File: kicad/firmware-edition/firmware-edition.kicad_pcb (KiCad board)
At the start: 2 copper layers, 70.4 x 63.5 mm, 102 parts, among them J1 Solar Panel, J10 GPIO, J11 I2C-3V3, J12 GPIO, J13 SPI, J14 I2C-5V, J15 SWD, J16 Conn_01x03, J17 Conn_01x01_Pin, J18 Conn_01x01_Pin, J19 Conn_01x01_Pin, J2 BATT, J20 Conn_01x01_Pin, J21 GPIO, J22 3V3, J3 3V3 Sensor Bus, J5 Conn_01x01_Pin, J6 Conn_01x01_Pin, J8 GPIO, J9 Conn_01x01_Pin, Q1 BSS84, Q2 BSS84, Q3 BSS84, SW1 BOOT_DFU, SW2 RST, U1 ADP5091, U2 TPS61023DRLR, U3 MAX-M10M-00B, U4 Si4463, U5 STM32U073KCU6, U6 TXS0102VDCTR, Y1 30MHz

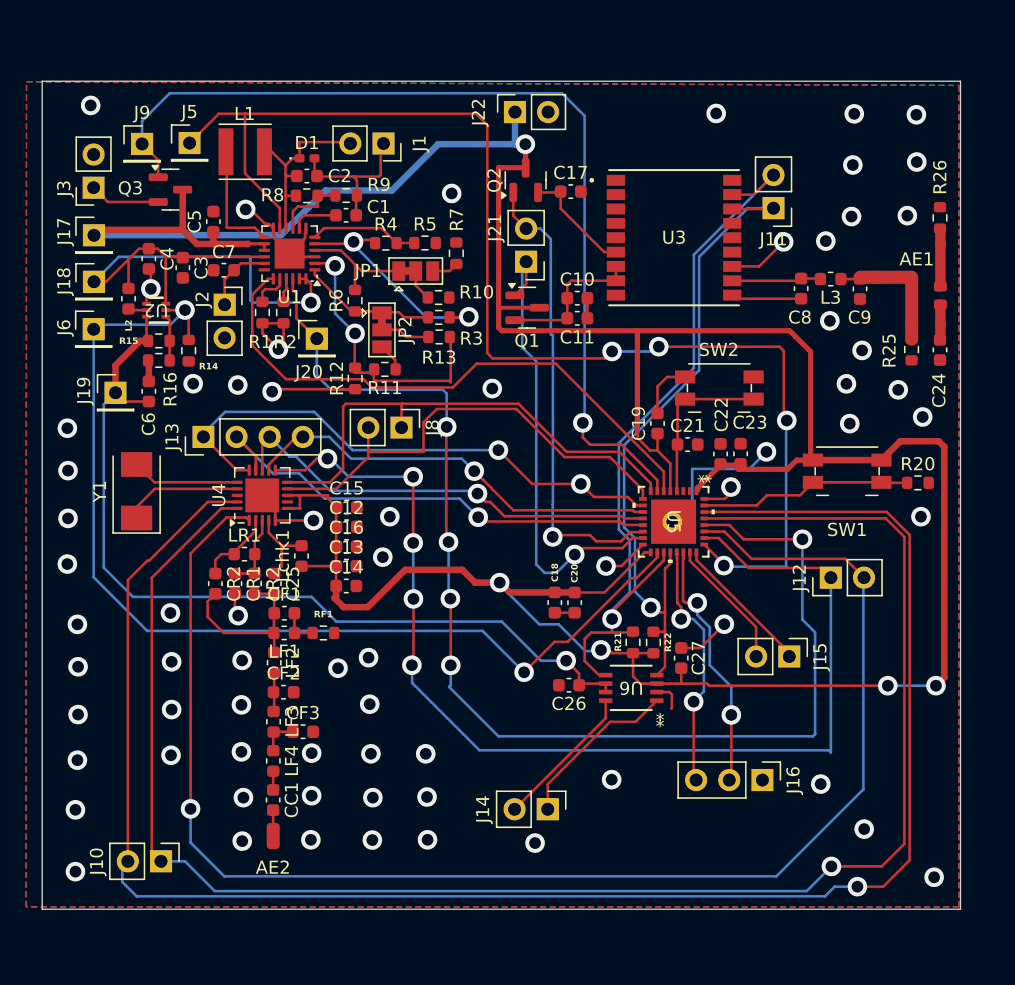
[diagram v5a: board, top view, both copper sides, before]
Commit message: main board updates, stm breakout
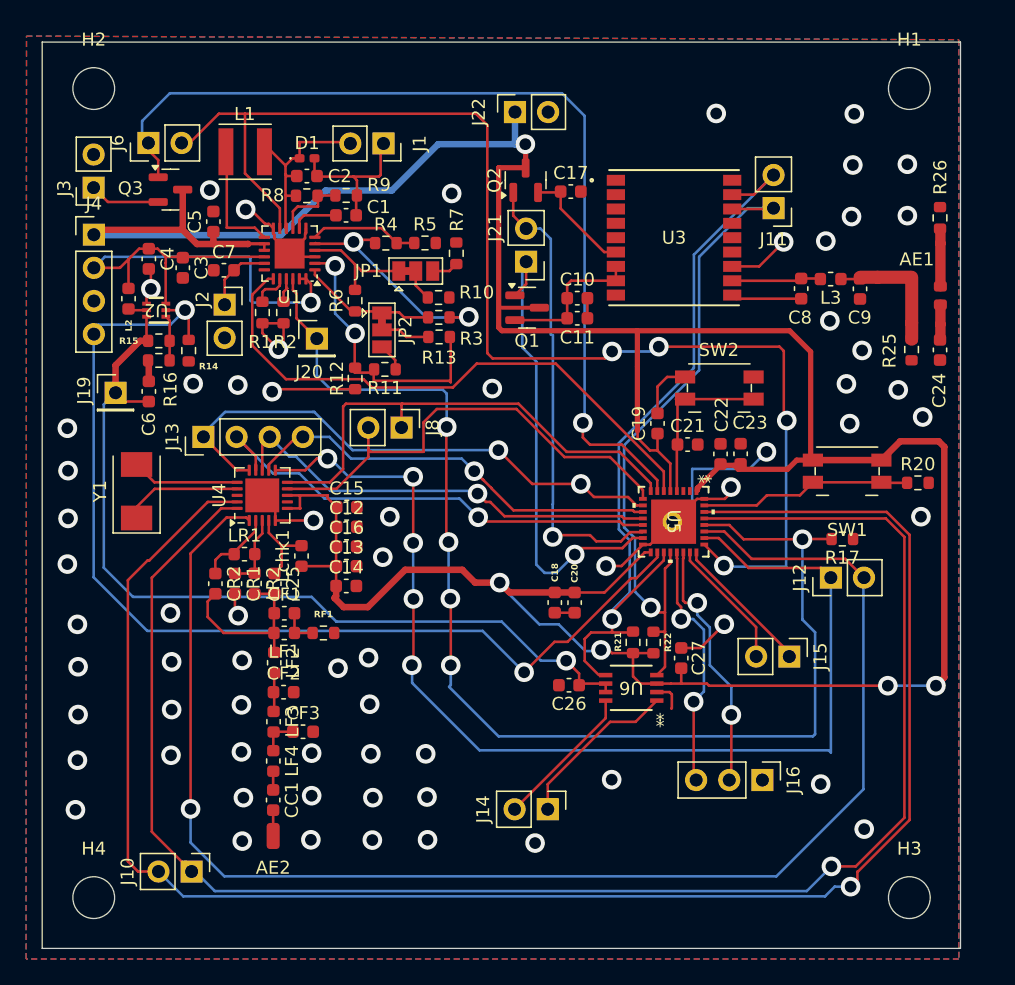
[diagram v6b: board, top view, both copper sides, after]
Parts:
- removed J17, J18, J5, J9: Conn_01x01_Pin, Connector_PinHeader_2.54mm:PinHeader_1x01_P2.54mm_Vertical
- added H1: MountingHole, MountingHole:MountingHole_3.2mm_M3_ISO14580, F.Cu at (175.0, 65.0)
- added H2: MountingHole, MountingHole:MountingHole_3.2mm_M3_ISO14580, F.Cu at (112.5, 65.0)
- added H3: MountingHole, MountingHole:MountingHole_3.2mm_M3_ISO14580, F.Cu at (175.0, 127.0)
- added H4: MountingHole, MountingHole:MountingHole_3.2mm_M3_ISO14580, F.Cu at (112.5, 127.0)
- added J4: Conn_01x04, Connector_PinHeader_2.54mm:PinHeader_1x04_P2.54mm_Vertical, F.Cu at (112.5, 76.2)
- added R17: 1M, Resistor_SMD:R_0603_1608Metric, F.Cu at (169.9, 99.5)
- J6: value Conn_01x01_Pin -> Conn_01x02; footprint Connector_PinHeader_2.54mm:PinHeader_1x01_P2.54mm_Vertical -> Connector_PinHeader_2.54mm:PinHeader_1x02_P2.54mm_Vertical
- moved J6 14.9 mm to (116.7, 69.2), turned to 90 degrees
- moved J10 2.47 mm to (120.0, 125.0)
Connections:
- net VSS renamed VSYS
- J6 pad 1: 5V_EN -> ~{SNSR_EN}
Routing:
- net GND: track 87.8 -> 91.2 mm, vias 69 -> 66
- net GPIO2: track 137.8 -> 135.0 mm
- net ~{CHRGR_EN}: track 94.4 -> 96.6 mm
- net GPIO3: track 129.6 -> 128.3 mm
- net VSYS: track 43.7 -> 42.6 mm
- net +3.3V: track 247.0 -> 246.4 mm
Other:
- board size 70.4 x 63.5 mm -> 70.4 x 69.4 mm

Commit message: Integration Boards V3.5
Fixed places prone to shorts and started adding header labels and fixing component labels on the silkscreen layer
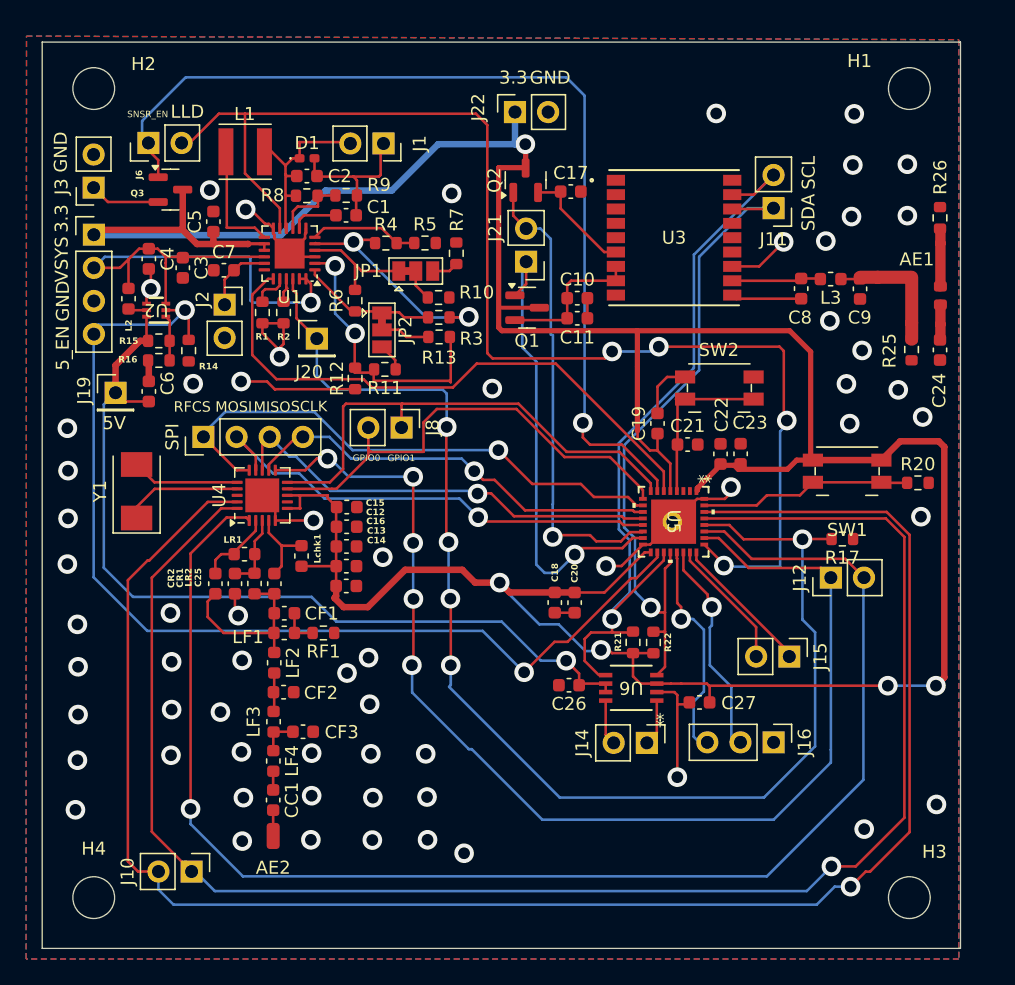
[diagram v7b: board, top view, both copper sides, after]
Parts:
- moved J14 9.14 mm to (154.9, 115.1)
- moved C27 3.67 mm to (158.9, 112.0), turned to 180 degrees
- moved J16 3.02 mm to (164.6, 115.1)
- renumbered J4 to 3.3, J13 to SPI
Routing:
- net /SDA_5V: track 12.9 -> 3.56 mm
- net /SCL_5V: track 11.2 -> 3.49 mm
- net ~{RF_IRQ}: track 85.9 -> 91.0 mm
- net ~{CHRGR_EN}: track 96.6 -> 101.1 mm
- net /USB_D+: track 19.9 -> 16.3 mm, vias 2 -> 1
- net /USB_D-: track 19.3 -> 16.6 mm, vias 2 -> 1
- net GND: track 91.2 -> 88.7 mm, vias 66 -> 62
- net ~{SNSR_EN}: track 72.9 -> 74.8 mm
- net GPIO2: track 135.0 -> 136.6 mm
- net ~{RF_EN}: track 113.2 -> 112.0 mm
- net ~{RF_CS}: track 41.9 -> 41.2 mm, vias 2 -> 1
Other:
- board text added: "3.3"
- board text added: "5V"
- board text added: "5_EN"
- board text added: "GND"
- board text added: "GPIO0"
- board text added: "GPIO1"
- board text added: "LLD"
- board text added: "MISO"
- board text added: "MOSI"
- board text added: "RFCS"
- board text added: "SCL"
- board text added: "SCLK"
- board text added: "SDA"
- board text added: "SNSR_EN"
- board text added: "VSYS"

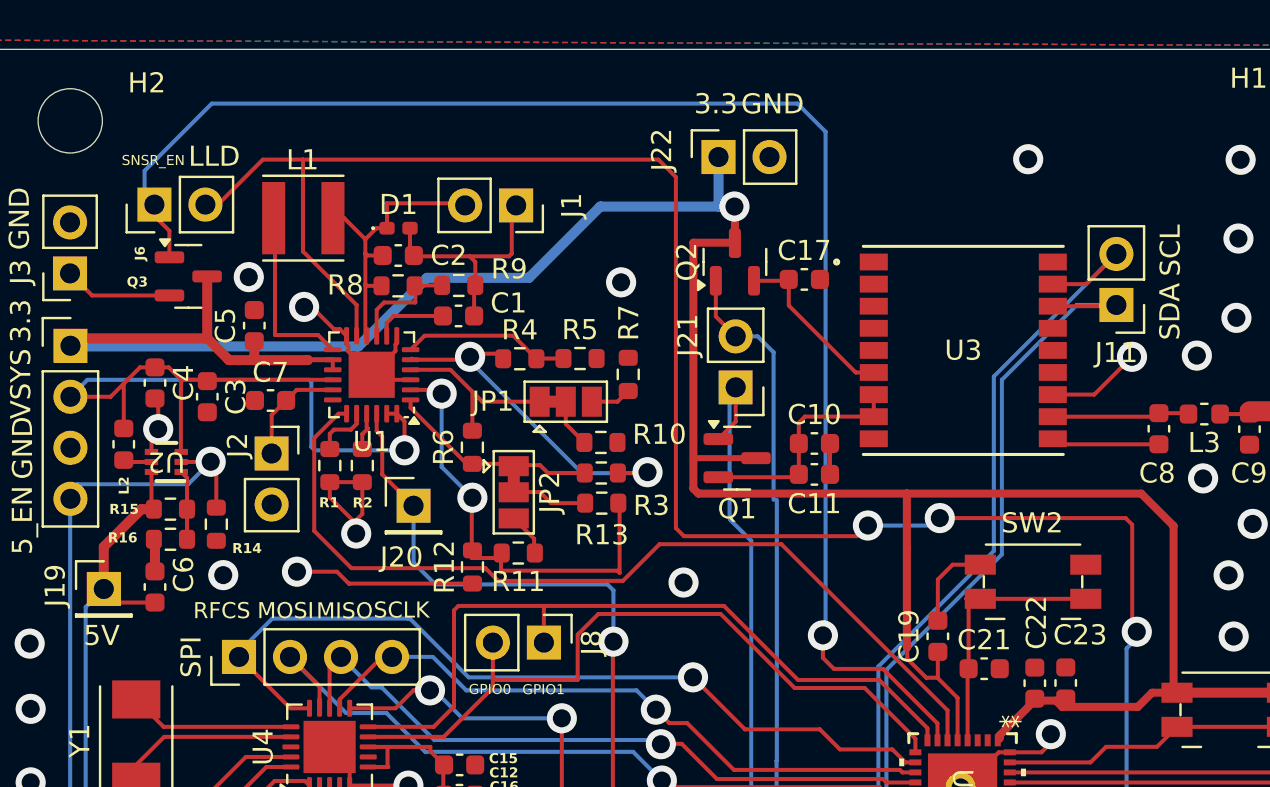
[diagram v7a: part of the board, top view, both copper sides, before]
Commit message: Silscreen layer fixed
Last Integrtion board V5
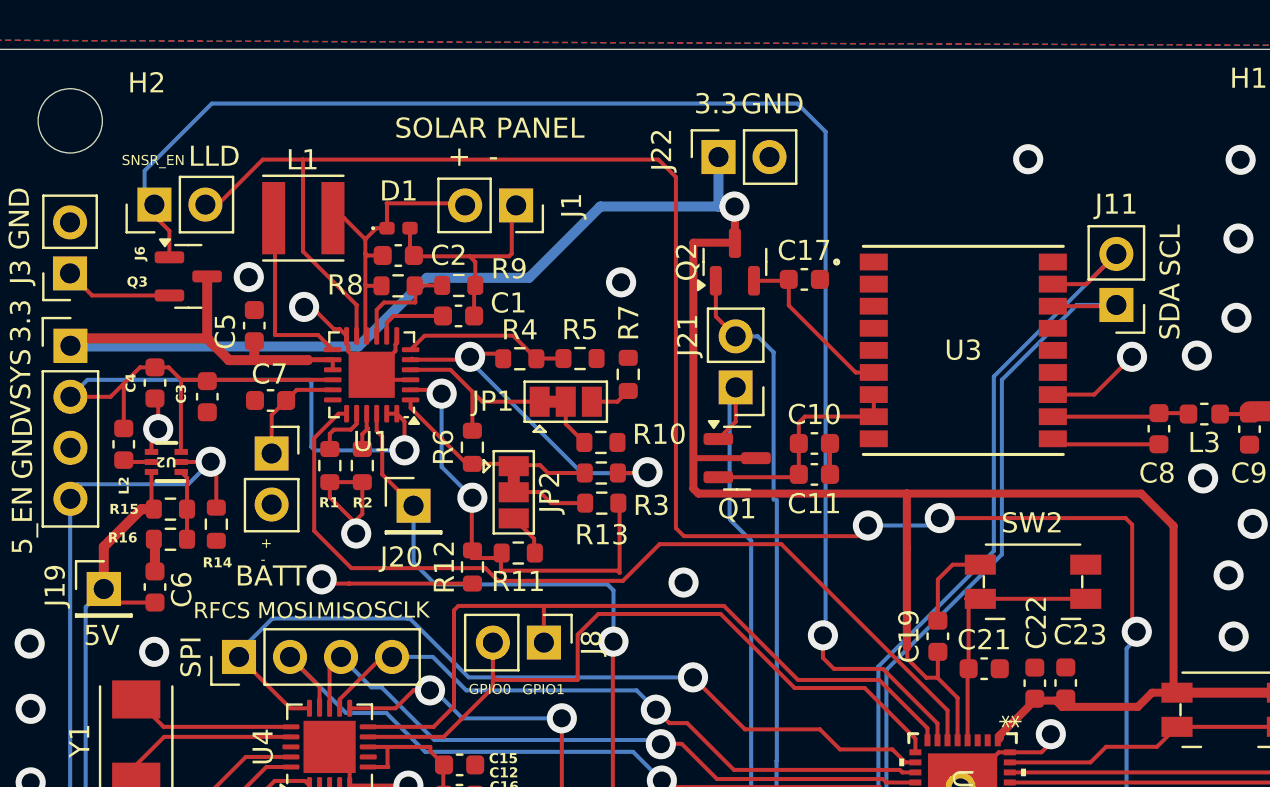
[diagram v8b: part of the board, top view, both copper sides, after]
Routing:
- net GND: track 88.7 -> 87.3 mm
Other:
- board text added: "+ -"
- board text added: "BATT"
- board text added: "SOLAR PANEL"
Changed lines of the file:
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@@
 		(tags "diode handsolder")
 		(property "Reference" "D1"
-			(at 0 -1.17 0)
+			(at 0.015 -1.845 0)
 			(layer "F.SilkS")
 			(effects
@@
 		(tags "capacitor")
 		(property "Reference" "C6"
-			(at 0.62 1.43 90)
+			(at -0.13 1.34 90)
 			(layer "F.SilkS")
 			(effects
@@
 		(tags "capacitor")
 		(property "Reference" "C3"
-			(at 0 -1.43 90)
+			(at -0.14058 1.295 90)
 			(layer "F.SilkS")
 			(effects
 				(font
-					(size 1 1)
-					(thickness 0.15)
+					(size 0.5 0.5)
+					(thickness 0.1)
+					(bold yes)
 				)
 			)
@@
 		(tags "resistor")
 		(property "Reference" "R14"
-			(at 1.205 -1.525 180)
+			(at 1.915 -0.055 180)
 			(layer "F.SilkS")
 			(effects
@@
 		(tags "capacitor")
 		(property "Reference" "C7"
-			(at 0 1.395 0)
+			(at 0.045 1.305 0)
 			(layer "F.SilkS")
 			(effects
@@
 			(effects
 				(font
-					(size 1 1)
-					(thickness 0.15)
+					(size 0.5 0.5)
+					(thickness 0.1)
+					(bold yes)
 				)
 			)
@@
 		(tags "capacitor")
 		(property "Reference" "C5"
-			(at 0 -1.43 90)
+			(at -0.293 -1.43 90)
 			(layer "F.SilkS")
 			(effects
@@
 			(at -1.69 -0.415 90)
 			(layer "F.SilkS")
+			(hide yes)
 			(effects
 				(font
@@
 		(tags "capacitor")
 		(property "Reference" "C4"
-			(at 0 -1.43 90)
+			(at 0 1.2 90)
 			(layer "F.SilkS")
 			(effects
 				(font
-					(size 1 1)
-					(thickness 0.15)
+					(size 0.5 0.5)
+					(thickness 0.1)
+					(bold yes)
 				)
 			)
@@
 		(tags "Through hole pin header THT 1x02 2.54mm single row")
 		(property "Reference" "J11"
-			(at 0 -2.38 0)
+			(at 0 5.008 0)
 			(layer "F.SilkS")
 			(effects
@@
 		)
 	)
+	(gr_text "BATT"
+		(at 120.71 88.26 0)
+		(layer "F.SilkS")
+		(effects
+			(font
+				(size 1 1)
+				(thickness 0.1)
+			)
+			(justify left bottom)
+		)
+	)
 	(gr_text "GND"
 		(at 110.56 71.44 90)
@@
 		)
 	)
+	(gr_text "+  -"
+		(at 131.3 67.36 0)
+		(layer "F.SilkS")
+		(effects
+			(font
+				(size 1 1)
+				(thickness 0.1)
+			)
+			(justify left bottom)
+		)
+	)
 	(gr_text "GPIO0"
 		(at 132.34 93.6 0)
@@
 		)
 	)
+	(gr_text "SOLAR PANEL"
+		(at 128.65 65.96 0)
+		(layer "F.SilkS")
+		(effects
+			(font
+				(size 1 1)
+				(thickness 0.15)
+			)
+			(justify left bottom)
+		)
+	)
 	(gr_text "GPIO1"
 		(at 135.01 93.61 0)
@@
 		)
 	)
+	(gr_text "+\n-"
+		(at 121.98 87.13 0)
+		(layer "F.SilkS")
+		(effects
+			(font
+				(size 0.5 0.5)
+				(thickness 0.1)
+			)
+			(justify left bottom)
+		)
+	)
 	(gr_text "SDA"
 		(at 167.85 75.93 90)
@@
 	)
 	(segment
-		(start 126.74 85.55)
-		(end 126.74 85.06)
+		(start 126.37 88.04)
+		(end 126.39 88.06)
 		(width 0.2)
 		(layer "F.Cu")
@@
 	)
 	(segment
-		(start 132.67 73.195)
-		(end 132.67 72.03)
+		(start 126.74 85.55)
+		(end 126.74 85.06)
 		(width 0.2)
 		(layer "F.Cu")
@@
 	)
 	(segment
-		(start 123.79 87.45)
-		(end 125.78 87.45)
+		(start 132.67 73.195)
+		(end 132.67 72.03)
 		(width 0.2)
 		(layer "F.Cu")
@@
 	)
 	(segment
-		(start 126.41 88.04)
-		(end 132.53 88.04)
-		(width 0.2)
-		(layer "F.Cu")
-		(net 1)
-	)
-	(segment
 		(start 157.22 117.77)
 		(end 157.22 112.19)
@@
 	)
 	(segment
-		(start 126.39 88.06)
-		(end 126.41 88.04)
-		(width 0.2)
-		(layer "F.Cu")
-		(net 1)
-	)
-	(segment
 		(start 129.65 71.745)
 		(end 129.61 71.705)
@@
 	)
 	(segment
-		(start 125.78 87.45)
-		(end 126.39 88.06)
-		(width 0.2)
-		(layer "F.Cu")
-		(net 1)
-	)
-	(segment
 		(start 125.6325 75.3725)
 		(end 125.925 75.3725)
@@
 	)
 	(segment
+		(start 126.41 88.04)
+		(end 132.53 88.04)
+		(width 0.2)
+		(layer "F.Cu")
+		(net 1)
+	)
+	(segment
 		(start 159.285 96.445001)
 		(end 158.732999 96.445001)
@@
 	)
 	(segment
+		(start 125.23 88.04)
+		(end 126.37 88.04)
+		(width 0.2)
+		(layer "F.Cu")
+		(net 1)
+	)
+	(segment
 		(start 154.585 99.944999)
 		(end 155.137001 99.944999)
@@
 	)
 	(segment
+		(start 125.02 87.83)
+		(end 125.23 88.04)
+		(width 0.2)
+		(layer "F.Cu")
+		(net 1)
+	)
+	(segment
 		(start 123.32 103.715)
 		(end 123.32 105.14)
@@
 		(net 1)
 	)
+	(segment
+		(start 126.39 88.06)
+		(end 126.41 88.04)
+		(width 0.2)
+		(layer "F.Cu")
+		(net 1)
+	)
 	(via
 		(at 137.94 115.98)
@@
 	)
 	(via
-		(at 123.79 87.45)
+		(at 125.02 87.83)
 		(size 1.5)
 		(drill 0.9)
@@
 	)
 	(via
-		(at 120.12 87.62)
+		(at 116.68 91.44)
 		(size 1.5)
 		(drill 0.9)
